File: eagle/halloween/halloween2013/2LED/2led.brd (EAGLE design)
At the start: 39.4 x 7.6 mm, 5 parts

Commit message: Update halloween
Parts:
- added E$3, E$5, E$7: (no value), con-molex:22-23-2021
- added E$4, E$6, E$8: (no value), adafruit:0207/10
- added LED3, LED4, LED5, LED6, LED7, LED8: (no value), led:LED3MM
- added R2, R3, R4: 1K, smd-ipc:R1206
- moved LED2 8.98 mm to (44.5, 5.08)
- moved E$1 1.27 mm to (25.4, 5.08)
- moved E$2 1.27 mm to (14.0, 5.08)
- moved LED1 1.27 mm to (3.81, 5.08)
- moved R1 1.27 mm to (14.3, 4.76)
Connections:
- new net S$10: E$5.2, LED6.A
- new net S$11: E$6.1, LED5.K, R3.2
- new net S$12: LED5.A, LED6.K
- new net S$13: E$7.1, E$8.2, R4.1
- new net S$14: E$7.2, LED8.A
- new net S$15: E$8.1, LED7.K, R4.2
- new net S$16: LED7.A, LED8.K
- new net S$2: E$3.1, E$4.2, R2.1
- new net S$6: E$3.2, LED4.A
- new net S$7: E$4.1, LED3.K, R2.2
- new net S$8: LED3.A, LED4.K
- new net S$9: E$5.1, E$6.2, R3.1
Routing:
- net S$12: track 0.00 -> 45.7 mm
- net S$8: track 0.00 -> 45.7 mm
- net S$16: track 0.00 -> 45.7 mm
- net S$6: track 0.00 -> 16.5 mm
- net S$14: track 0.00 -> 16.5 mm
- net S$10: track 0.00 -> 16.5 mm
- net S$7: track 0.00 -> 15.7 mm
- net S$11: track 0.00 -> 15.7 mm
- net S$15: track 0.00 -> 15.7 mm
- net S$5: track 7.62 -> 16.5 mm
- net S$3: track 36.8 -> 45.7 mm
- net S$9: track 0.00 -> 8.74 mm
- net S$2: track 0.00 -> 8.74 mm
- net S$13: track 0.00 -> 8.74 mm
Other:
- board size 39.4 x 7.6 mm -> 49 x 45.7 mm

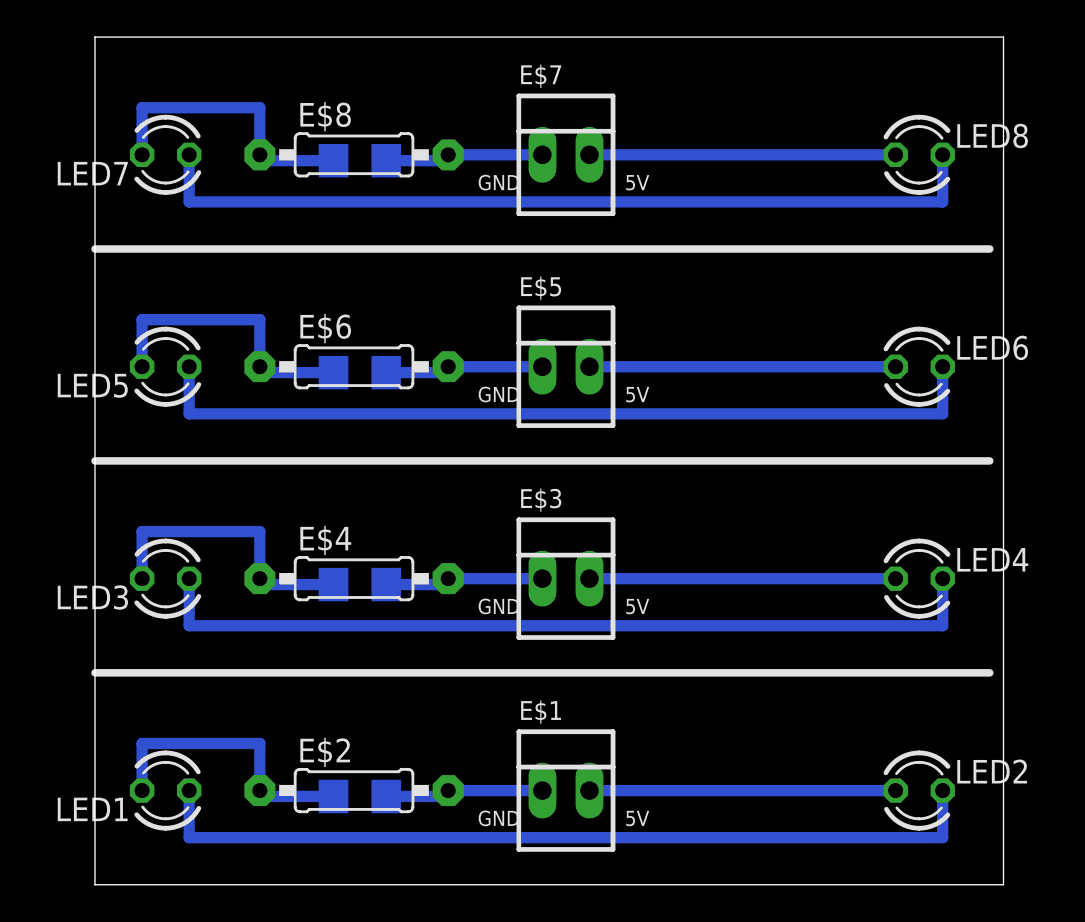
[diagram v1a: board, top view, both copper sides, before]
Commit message: Update 2D led file
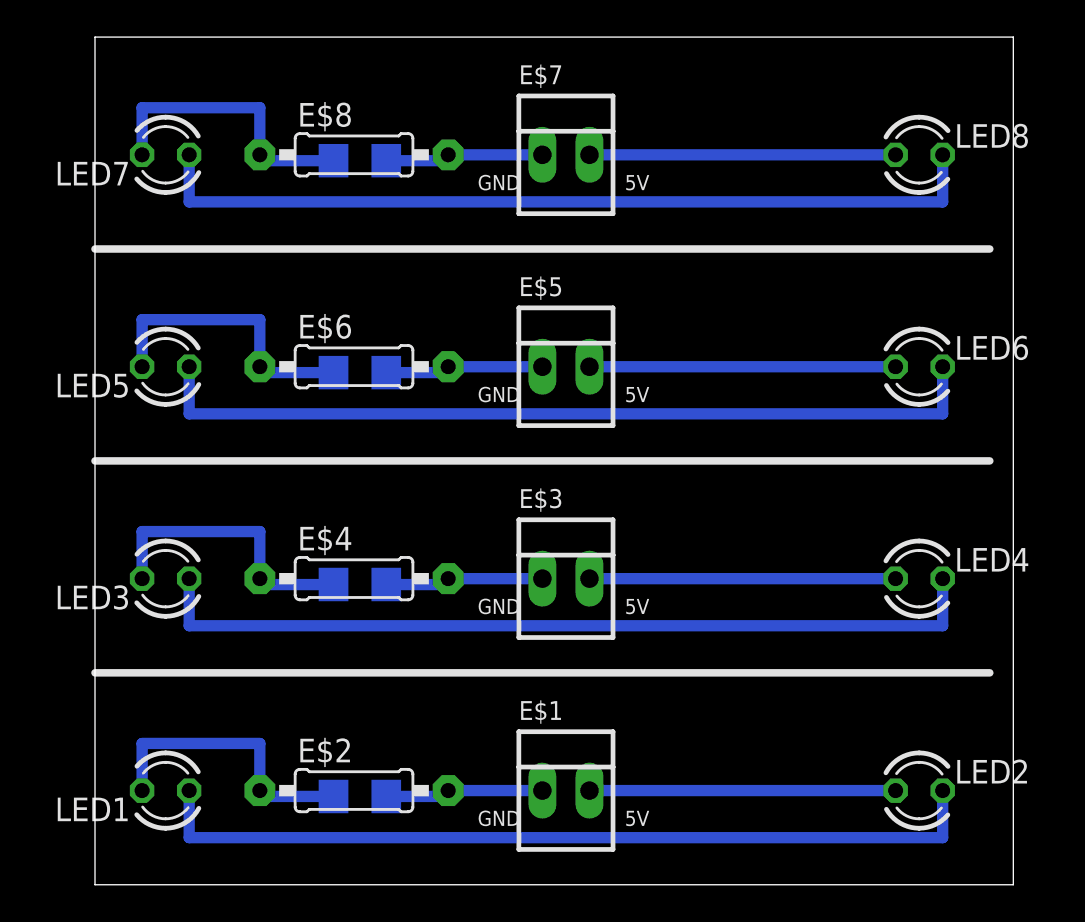
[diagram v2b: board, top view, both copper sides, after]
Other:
- board size 49 x 45.7 mm -> 49.5 x 45.7 mm
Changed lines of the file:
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@@
 <?xml version="1.0" encoding="utf-8"?>
 <!DOCTYPE eagle SYSTEM "eagle.dtd">
-<eagle version="6.4">
+<eagle version="6.1">
 <drawing>
 <settings>
@@
 <layer number="18" name="Vias" color="2" fill="1" visible="yes" active="yes"/>
 <layer number="19" name="Unrouted" color="6" fill="1" visible="yes" active="yes"/>
-<layer number="20" name="Dimension" color="12" fill="0" visible="yes" active="yes"/>
+<layer number="20" name="Dimension" color="15" fill="1" visible="yes" active="yes"/>
 <layer number="21" name="tPlace" color="15" fill="1" visible="yes" active="yes"/>
 <layer number="22" name="bPlace" color="7" fill="1" visible="yes" active="yes"/>
@@
 <text x="20.6375" y="3.175" size="0.8128" layer="21" ratio="4">GND</text>
 <text x="28.575" y="3.175" size="0.8128" layer="21" ratio="4">5V</text>
-<rectangle x1="0" y1="0" x2="49" y2="45.72" layer="20"/>
 <wire x1="0" y1="11.43" x2="48.26" y2="11.43" width="0.4064" layer="25"/>
 <wire x1="0" y1="22.86" x2="48.26" y2="22.86" width="0.4064" layer="25"/>
@@
 <text x="20.6375" y="37.465" size="0.8128" layer="21" ratio="4">GND</text>
 <text x="28.575" y="37.465" size="0.8128" layer="21" ratio="4">5V</text>
+<wire x1="0" y1="0" x2="0" y2="45.72" width="0" layer="20"/>
+<wire x1="0" y1="45.72" x2="49.53" y2="45.72" width="0" layer="20"/>
+<wire x1="49.53" y1="45.72" x2="49.53" y2="0" width="0" layer="20"/>
+<wire x1="49.53" y1="0" x2="0" y2="0" width="0" layer="20"/>
 </plain>
 <attributes>
@@
 </class>
 </classes>
-<designrules name="default">
+<designrules>
 <description language="de">&lt;b&gt;EAGLE Design Rules&lt;/b&gt;
 &lt;p&gt;
